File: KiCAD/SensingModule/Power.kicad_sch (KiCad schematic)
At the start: 7 parts, among them U2 NJM7805SDL1

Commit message: MKRWAN問題解決
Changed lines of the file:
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@@
+		(color 0 0 0 0)
+	)
+	(junction
+		(at 92.71 50.8)
+		(diameter 0)
 		(color 0 0 0 0)
 	)
@@
 					(unit 1)
 				)
+			)
+		)
+	)
+	(symbol
+		(lib_id "power:PWR_FLAG")
+		(at 92.71 50.8 0)
+		(unit 1)
+		(exclude_from_sim no)
+		(in_bom yes)
+		(on_board yes)
+		(dnp no)
+		(fields_autoplaced yes)
+		(property "Reference" "#FLG03"
+			(at 92.71 48.895 0)
+			(effects
+				(font
+					(size 1.27 1.27)
+				)
+				(hide yes)
+			)
+		)
+		(property "Value" "PWR_FLAG"
+			(at 92.71 45.72 0)
+			(effects
+				(font
+					(size 1.27 1.27)
+				)
+			)
+		)
+		(property "Footprint" ""
+			(at 92.71 50.8 0)
+			(effects
+				(font
+					(size 1.27 1.27)
+				)
+				(hide yes)
+			)
+		)
+		(property "Datasheet" "~"
+			(at 92.71 50.8 0)
+			(effects
+				(font
+					(size 1.27 1.27)
+				)
+				(hide yes)
+			)
+		)
+		(property "Description" "Special symbol for telling ERC where power comes from"
+			(at 92.71 50.8 0)
+			(effects
+				(font
+					(size 1.27 1.27)
+				)
+				(hide yes)
+			)
+		)
+		(pin "1"
+		)
+		(instances
+			(project "SensingModule"
+				(path "/5f6205c9-e8e0-4a74-82d8-bdf647a68791/379d4819-b39f-40ef-ade3-95aa2eb84992"
+					(reference "#FLG03")
+					(unit 1)
+				)

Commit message: 配線作業終了、確認お願いします
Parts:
- U2: footprint Package_TO_SOT_SMD:TO-252-2 -> Connector_PinHeader_2.54mm:PinHeader_1x03_P2.54mm_Vertical
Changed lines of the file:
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@@
 			)
 		)
-		(property "Footprint" "Package_TO_SOT_SMD:TO-252-2"
+		(property "Footprint" "Connector_PinHeader_2.54mm:PinHeader_1x03_P2.54mm_Vertical"
 			(at 100.965 54.61 0)
 			(effects

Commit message: Sensingの配線作業終わり、確認お願いします。
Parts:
- U2: footprint Connector_PinHeader_2.54mm:PinHeader_1x03_P2.54mm_Vertical -> TSRP_IC:M78AR03305
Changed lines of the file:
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@@
 			)
 		)
-		(property "Footprint" "Connector_PinHeader_2.54mm:PinHeader_1x03_P2.54mm_Vertical"
+		(property "Footprint" "TSRP_IC:M78AR03305"
 			(at 100.965 54.61 0)
 			(effects

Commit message: 配線確認お願いします
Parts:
- D3: value R -> Greeen
- R10: value 2.4kR -> 2.2kR
- U2: value NJM7805SDL1 -> M78AR03305
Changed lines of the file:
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@@
 			)
 		)
-		(property "Value" "NJM7805SDL1"
+		(property "Value" "M78AR03305"
 			(at 100.33 46.99 0)
 			(effects
@@
 			)
 		)
-		(property "Value" "2.4kR"
+		(property "Value" "2.2kR"
 			(at 54.61 48.895 0)
 			(effects
@@
 			)
 		)
-		(property "Value" "R"
+		(property "Value" "Greeen"
 			(at 54.61 56.4515 90)
 			(effects

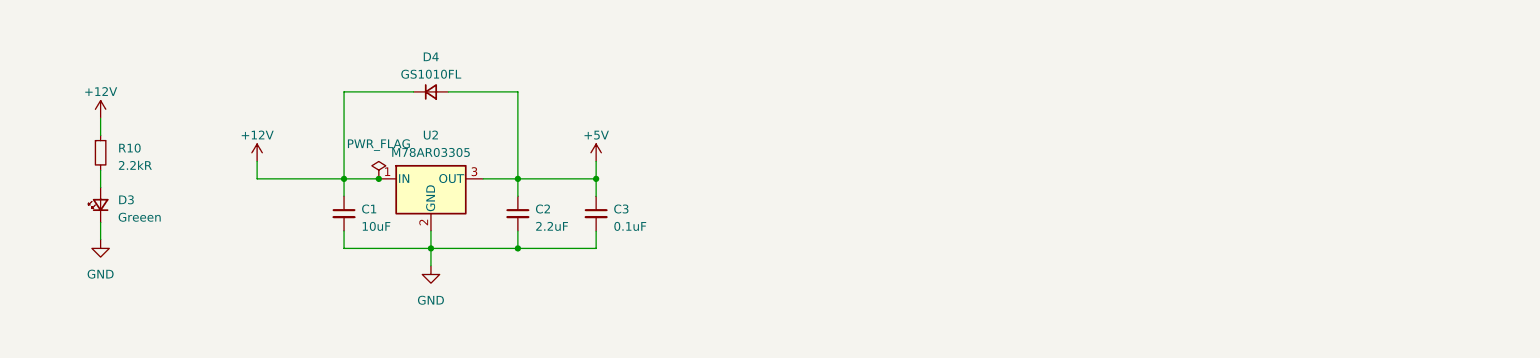
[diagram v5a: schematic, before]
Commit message: 電源部に保護を追加．DRCエラー無し．
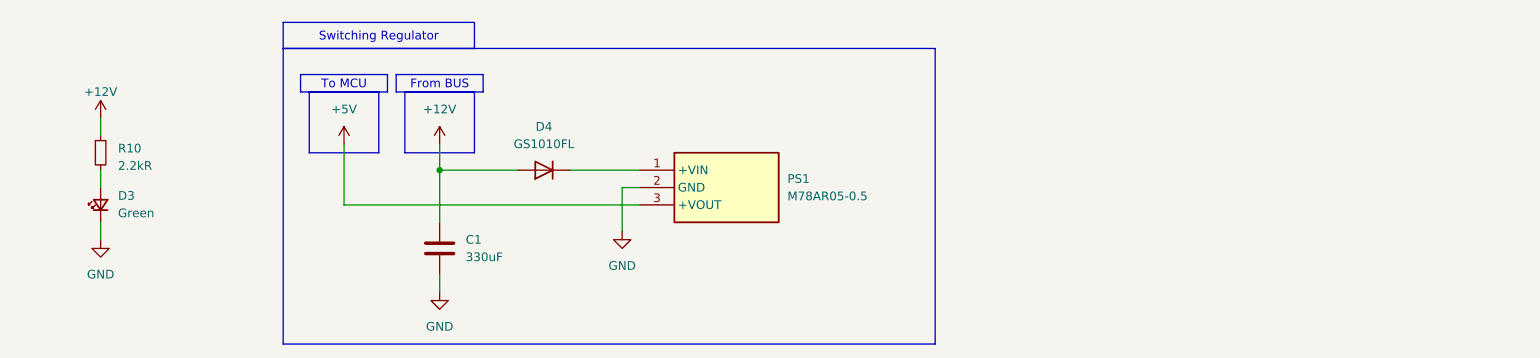
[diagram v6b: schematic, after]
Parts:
- removed C1: 10uF, Capacitor_SMD:C_1206_3216Metric_Pad1.33x1.80mm_HandSolder, symbol Device:C_Small
- removed C2: 2.2uF, Capacitor_SMD:C_0603_1608Metric_Pad1.08x0.95mm_HandSolder, symbol Device:C_Small
- removed C3: 0.1uF, Capacitor_SMD:C_0603_1608Metric_Pad1.08x0.95mm_HandSolder, symbol Device:C_Small
- removed D4: GS1010FL, Diode_SMD:D_SOD-123F, symbol Device:D_Small
- removed U2: M78AR03305, TSRP_IC:M78AR03305, symbol Regulator_Linear:L7805
- added C1: 330uF, Capacitor_SMD:CP_Elec_10x10, symbol Device:C
- added D4: GS1010FL, Diode_SMD:D_SOD-123F, symbol Device:D
- added PS1: M78AR05-0.5, TSRP_IC:M78AR03305, symbol TSRP_IC:M78AR05-0.5
- D3: value Greeen -> Green
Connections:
- net +12V: now also C1.2, D4.2 (A)
- net +5V: now also PS1.3 (+VOUT)
- net GND: now also C1.1, PS1.2 (GND)
- new net: D4.1 (K), PS1.1 (+VIN)

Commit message: きれいに配線できるようになった．
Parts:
- removed D4: GS1010FL, Diode_SMD:D_SOD-123F, symbol Device:D
- added C10, C11: 1uF, Capacitor_SMD:C_0805_2012Metric_Pad1.18x1.45mm_HandSolder, symbol Device:C
- added D7: SB34AFC, Diode_SMD:D_SMA_Handsoldering, symbol Device:D_Schottky
- added U8: NCV8114BSN330T1G, Package_TO_SOT_SMD:TSOT-23-5, symbol Regulator_Linear:NCV8114BSN330T1G
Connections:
- net +12V: now also D7.2 (A)
- net +5V: now also C10.1, U8.1 (IN), U8.3 (EN)
- net GND: now also C10.2, C11.2, U8.2 (GND)
- net at PS1.1 (+VIN): now also D7.1 (K)
- new net +3.3VP: C11.1, U8.5 (OUT)
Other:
- note added: "本当は RT9080-33GJ5"
- note added: "逆接続保護ダイオード"

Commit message: Build-2完成．発注．
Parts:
- C1: symbol Device:C -> Device:C_Polarized
- U8: value NCV8114BSN330T1G -> RT9080-33GJ5
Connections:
- net +12V: now also C1.1; no longer C1.2
- net GND: now also C1.2; no longer C1.1
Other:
- moved on the sheet: D3, D7, PS1, R10
